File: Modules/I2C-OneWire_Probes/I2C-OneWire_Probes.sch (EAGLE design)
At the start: 25 parts, among them J1 QWIIC_RIGHT_ANGLE, Q1 AO3401, Q2 AO3401, Q3 AO3401, U1 AMS1117-3.3

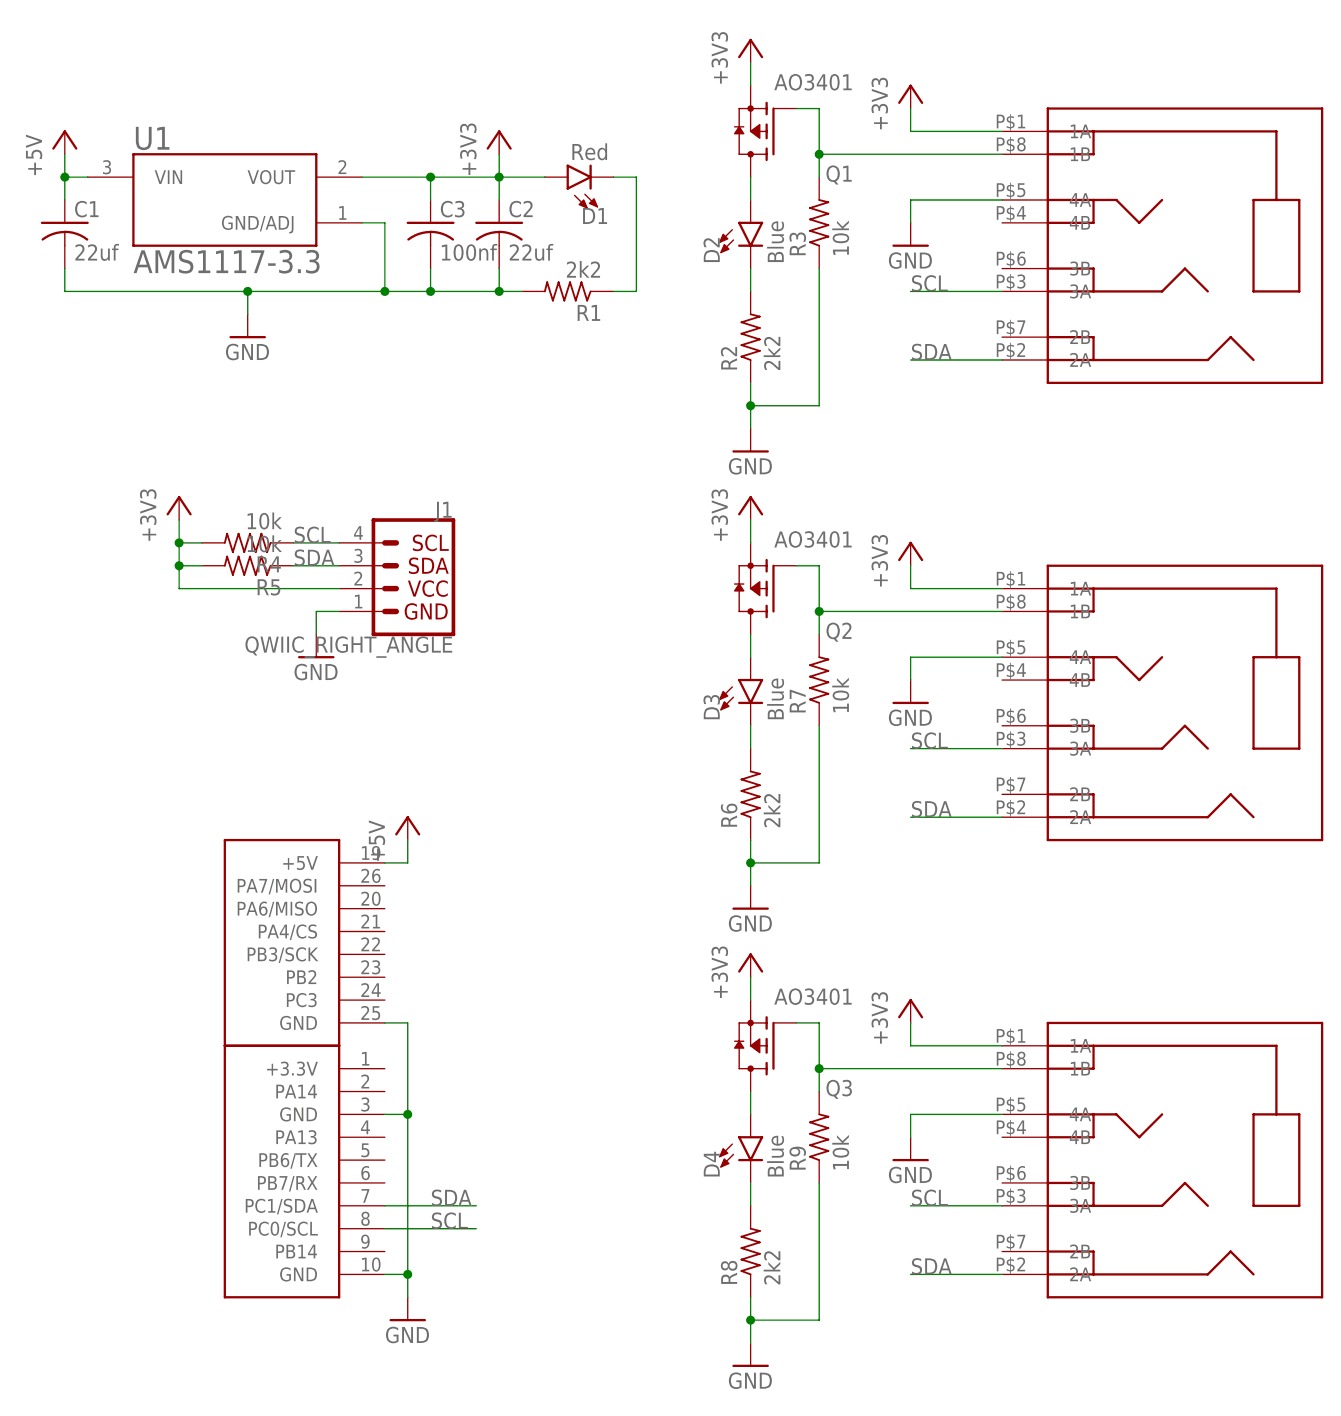
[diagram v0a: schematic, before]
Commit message: fixed pinout for 3.5mm jacks on I2C-OneWire-Probes
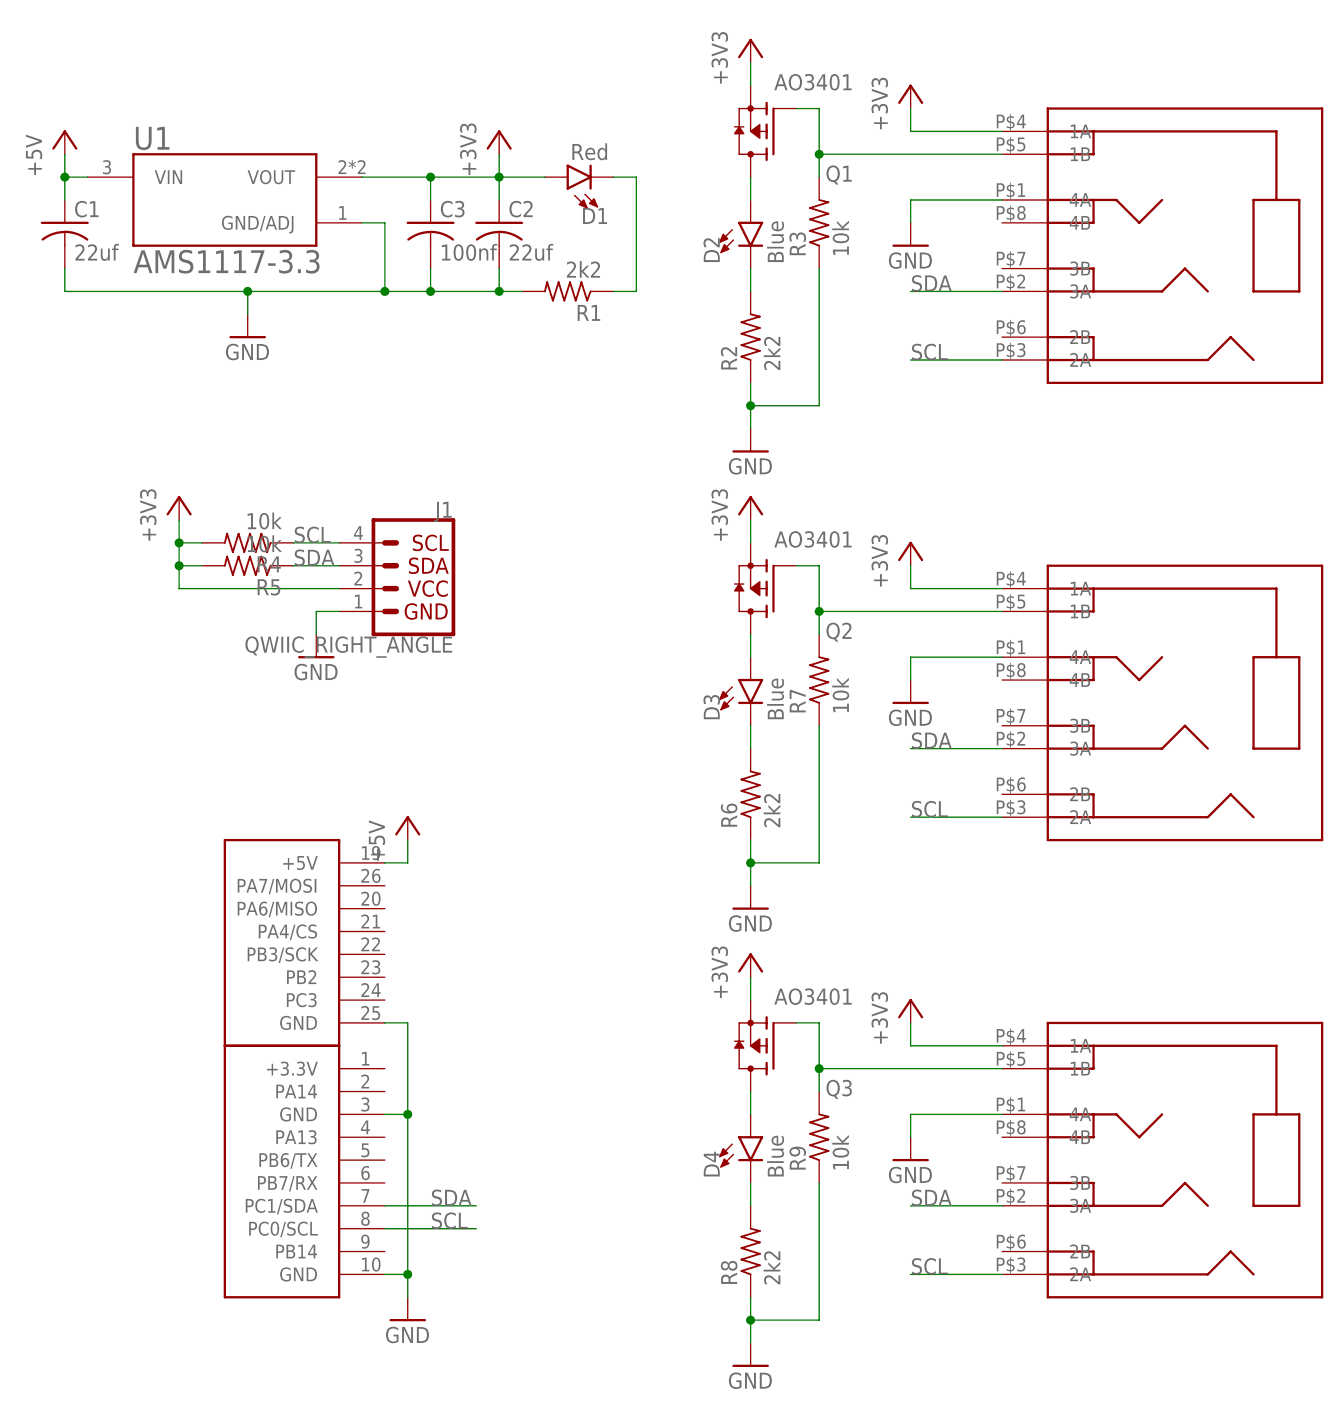
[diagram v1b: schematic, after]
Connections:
- net SCL: now also U$2.2A, U$3.2A, U$4.2A; no longer U$2.3A, U$3.3A, U$4.3A
- net SDA: now also U$2.3A, U$3.3A, U$4.3A; no longer U$2.2A, U$3.2A, U$4.2A
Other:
- moved on the sheet: U1
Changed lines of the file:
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@@
 <net name="SCL" class="0">
-<segment>
-<pinref part="U$2" gate="G$1" pin="3A"/>
-<wire x1="180.34" y1="93.98" x2="170.18" y2="93.98" width="0.1524" layer="91"/>
-<label x="170.18" y="93.98" size="1.778" layer="95"/>
-</segment>
 <segment>
 <pinref part="J1" gate="J1" pin="4"/>
@@
 <label x="101.6" y="66.04" size="1.778" layer="95"/>
 <pinref part="R4" gate="G$1" pin="1"/>
+</segment>
+<segment>
+<pinref part="U$1" gate="G$2" pin="PC0/SCL"/>
+<wire x1="111.76" y1="-10.16" x2="121.92" y2="-10.16" width="0.1524" layer="91"/>
+<label x="116.84" y="-10.16" size="1.778" layer="95"/>
+</segment>
+<segment>
+<pinref part="U$2" gate="G$1" pin="2A"/>
+<wire x1="180.34" y1="86.36" x2="170.18" y2="86.36" width="0.1524" layer="91"/>
+<label x="170.18" y="86.36" size="1.778" layer="95"/>
+</segment>
+<segment>
+<pinref part="U$3" gate="G$1" pin="2A"/>
+<wire x1="180.34" y1="35.56" x2="170.18" y2="35.56" width="0.1524" layer="91"/>
+<label x="170.18" y="35.56" size="1.778" layer="95"/>
+</segment>
+<segment>
+<pinref part="U$4" gate="G$1" pin="2A"/>
+<wire x1="180.34" y1="-15.24" x2="170.18" y2="-15.24" width="0.1524" layer="91"/>
+<label x="170.18" y="-15.24" size="1.778" layer="95"/>
+</segment>
+</net>
+<net name="SDA" class="0">
+<segment>
+<pinref part="J1" gate="J1" pin="3"/>
+<wire x1="106.68" y1="63.5" x2="101.6" y2="63.5" width="0.1524" layer="91"/>
+<label x="101.6" y="63.5" size="1.778" layer="95"/>
+<pinref part="R5" gate="G$1" pin="1"/>
+</segment>
+<segment>
+<pinref part="U$1" gate="G$2" pin="PC1/SDA"/>
+<wire x1="111.76" y1="-7.62" x2="121.92" y2="-7.62" width="0.1524" layer="91"/>
+<label x="116.84" y="-7.62" size="1.778" layer="95"/>
+</segment>
+<segment>
+<pinref part="U$2" gate="G$1" pin="3A"/>
+<wire x1="180.34" y1="93.98" x2="170.18" y2="93.98" width="0.1524" layer="91"/>
+<label x="170.18" y="93.98" size="1.778" layer="95"/>
 </segment>
 <segment>
@@
 <label x="170.18" y="-7.62" size="1.778" layer="95"/>
 </segment>
-<segment>
-<pinref part="U$1" gate="G$2" pin="PC0/SCL"/>
-<wire x1="111.76" y1="-10.16" x2="121.92" y2="-10.16" width="0.1524" layer="91"/>
-<label x="116.84" y="-10.16" size="1.778" layer="95"/>
-</segment>
 </net>
-<net name="SDA" class="0">
-<segment>
-<pinref part="U$2" gate="G$1" pin="2A"/>
-<wire x1="180.34" y1="86.36" x2="170.18" y2="86.36" width="0.1524" layer="91"/>
-<label x="170.18" y="86.36" size="1.778" layer="95"/>
-</segment>
-<segment>
-<pinref part="J1" gate="J1" pin="3"/>
-<wire x1="106.68" y1="63.5" x2="101.6" y2="63.5" width="0.1524" layer="91"/>
-<label x="101.6" y="63.5" size="1.778" layer="95"/>
-<pinref part="R5" gate="G$1" pin="1"/>
-</segment>
-<segment>
-<pinref part="U$3" gate="G$1" pin="2A"/>
-<wire x1="180.34" y1="35.56" x2="170.18" y2="35.56" width="0.1524" layer="91"/>
-<label x="170.18" y="35.56" size="1.778" layer="95"/>
-</segment>
-<segment>
-<pinref part="U$4" gate="G$1" pin="2A"/>
-<wire x1="180.34" y1="-15.24" x2="170.18" y2="-15.24" width="0.1524" layer="91"/>
-<label x="170.18" y="-15.24" size="1.778" layer="95"/>
-</segment>
-<segment>
-<pinref part="U$1" gate="G$2" pin="PC1/SDA"/>
-<wire x1="111.76" y1="-7.62" x2="121.92" y2="-7.62" width="0.1524" layer="91"/>
-<label x="116.84" y="-7.62" size="1.778" layer="95"/>
-</segment>
-</net>
